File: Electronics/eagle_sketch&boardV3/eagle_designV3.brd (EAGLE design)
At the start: 134.6 x 61.9 mm, 16 parts, among them IC1 7805L

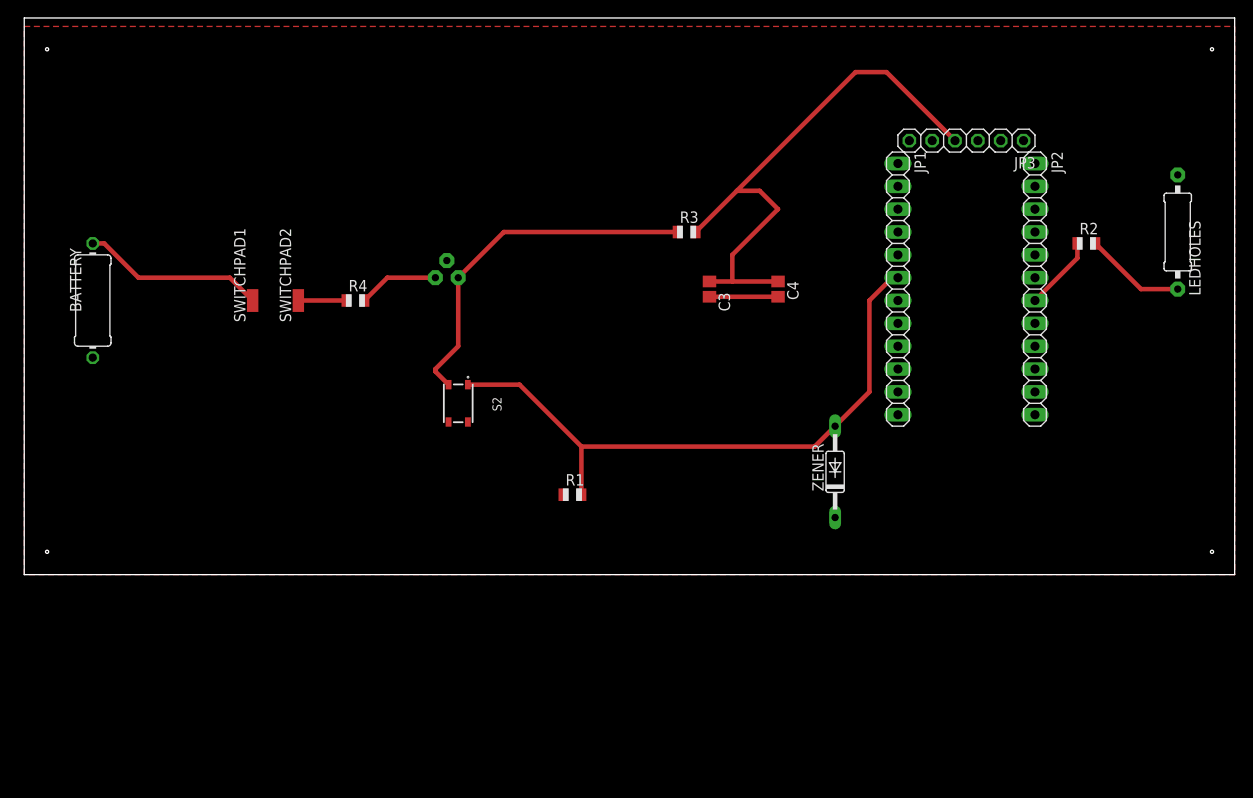
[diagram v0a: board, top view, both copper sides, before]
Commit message: updated board and schematic with post review suggestions from Issue 30
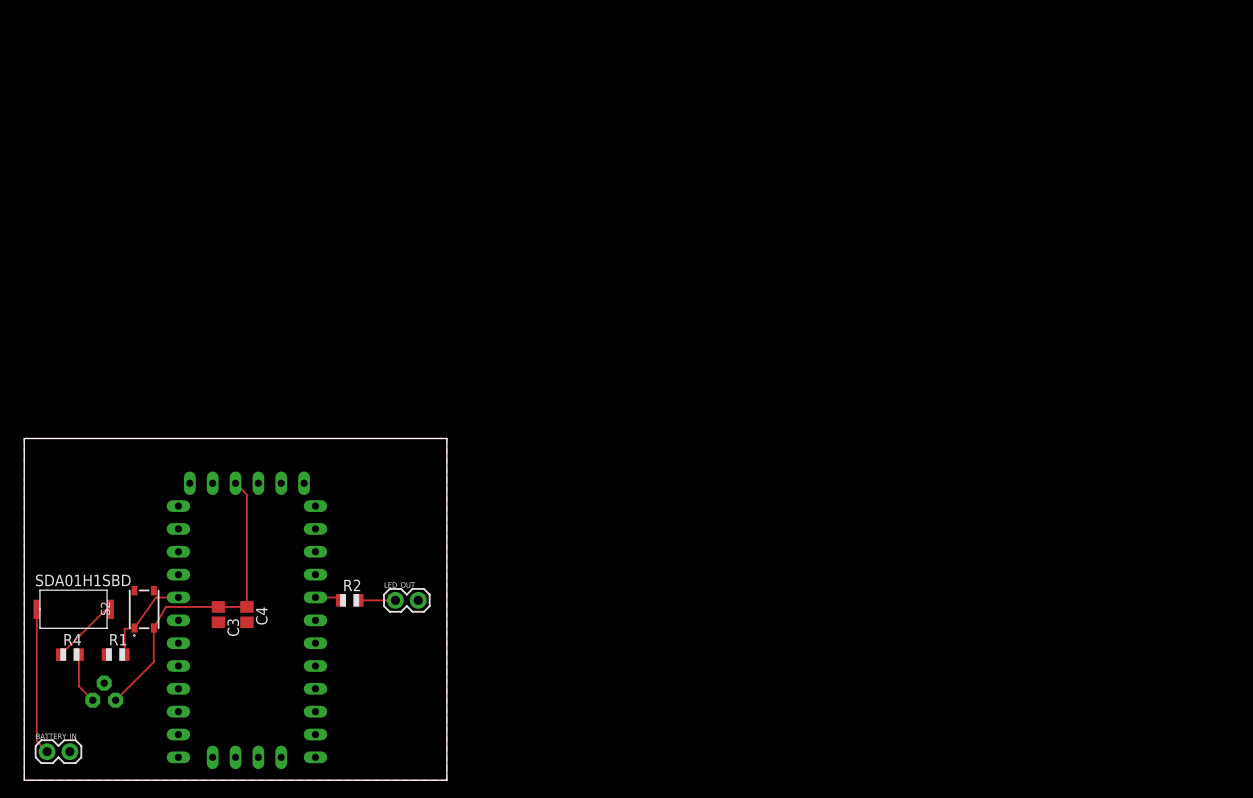
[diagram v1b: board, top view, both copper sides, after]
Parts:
- removed BATTERY: (no value), adafruit:0411/12
- removed JP1, JP2: (no value), adafruit:1X12
- removed JP3: (no value), adafruit:1X06
- removed LEDHOLES: (no value), adafruit:0309/12
- removed R3: 20k, adafruit:R0805
- removed SWITCHPAD1, SWITCHPAD2: (no value), wirepad:SMD1,27-2,54
- removed ZENER: 1N4446, diode:DO35-10
- added BATTERY_IN, LED_OUT: (no value), SparkFun-Connectors:1X02
- added U$1: PRO-MINI, Arduino-clone:PRO-MINI
- added U$2: SDA01H1SBD_DEVICE, DIPswitchLib:SDA01H1SBD_PART
- moved R2 91.0 mm to (36.2, 20.0)
- moved C4 69.3 mm to (24.8, 18.4)
- moved C3 65.5 mm to (21.6, 18.4)
- moved IC1 60.5 mm to (8.89, 8.89)
- moved R1 53.8 mm to (10.2, 14.0)
- moved R4 50.6 mm to (5.08, 14.0)
- moved S2 41.8 mm to (13.3, 19.0), turned to 90 degrees
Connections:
- removed net N$6: C3.1, C4.1, JP3.4, R3.2
- removed net N$9: LEDHOLES.2, R2.2
- new net N$7: LED_OUT.1, R2.2
- new net RAW: U$1.RAW
- net GND: now also BATTERY_IN.2, LED_OUT.2, U$1.GND; no longer BATTERY.1, JP2.2, LEDHOLES.1, ZENER.C
- net N$1: now also BATTERY_IN.1, U$2.OFF; no longer BATTERY.2, SWITCHPAD1.1
- net N$2: now also U$2.ON; no longer SWITCHPAD2.1
- net N$4: now also C3.1, C4.1, U$1.VCC1; no longer R3.1
- net N$5: now also U$1.D2; no longer JP1.6, ZENER.A
- net N$8: now also U$1.A3; no longer JP2.7
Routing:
- net N$6: track 62.6 -> 0.00 mm
- net N$5: track 69.8 -> 10.6 mm
- net N$9: track 11.3 -> 0.00 mm
- net GND: track 7.62 -> 0.00 mm
- net N$8: track 8.30 -> 2.94 mm
- net N$4: track 40.1 -> 35.8 mm
- net N$1: track 20.4 -> 16.3 mm
- net N$7: track 0.00 -> 4.08 mm
- net N$3: track 8.94 -> 5.72 mm
- net N$2: track 5.35 -> 8.32 mm
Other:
- board size 134.6 x 61.9 mm -> 47 x 38 mm

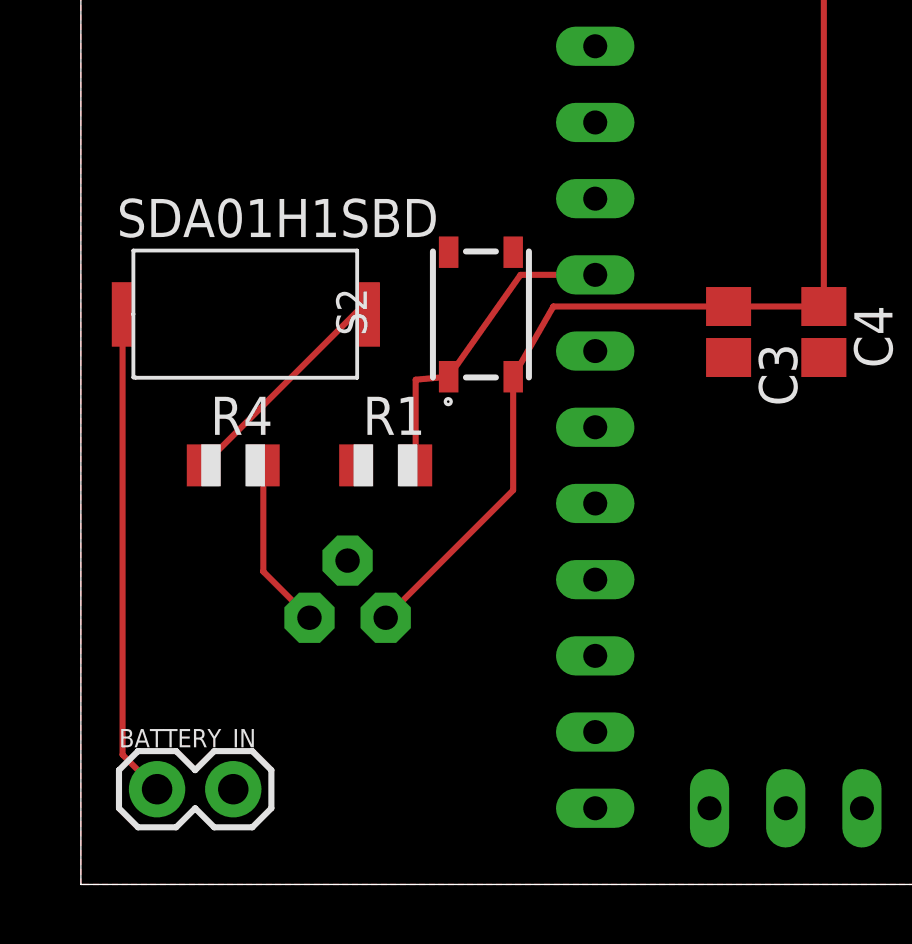
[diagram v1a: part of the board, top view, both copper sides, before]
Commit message: updated board to reflect toggle switch change
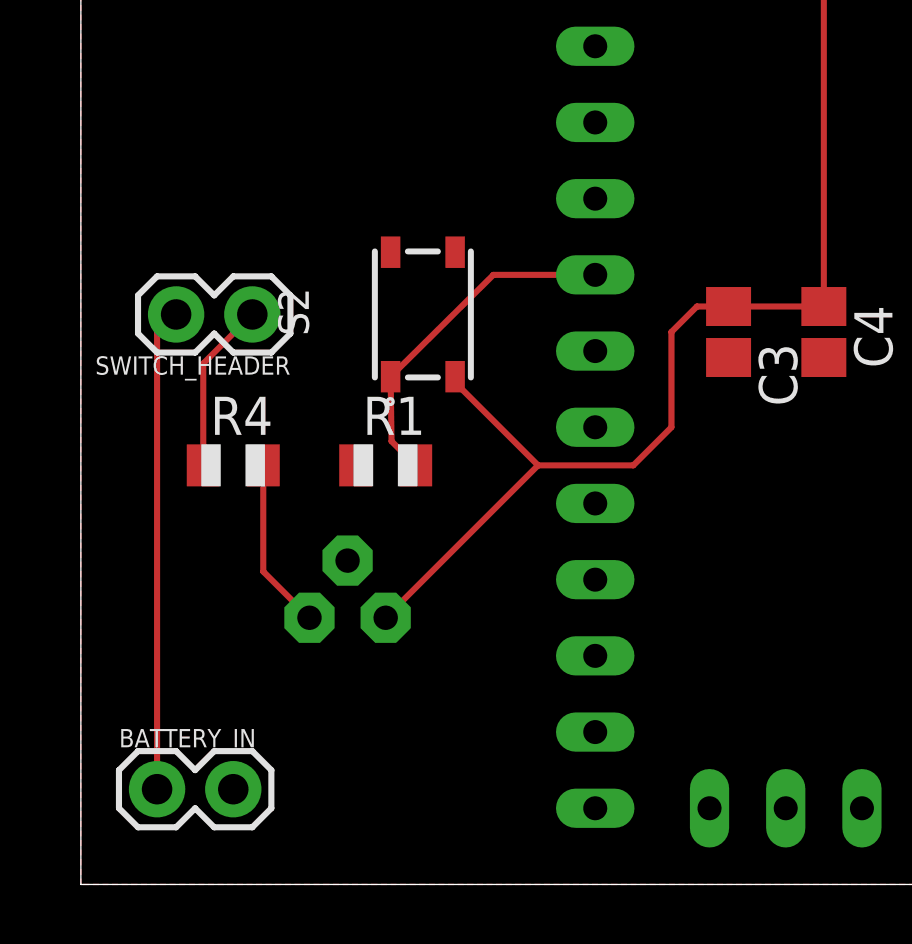
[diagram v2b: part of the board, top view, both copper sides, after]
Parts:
- removed U$2: SDA01H1SBD_DEVICE, DIPswitchLib:SDA01H1SBD_PART
- added SWITCH_HEADER: (no value), SparkFun-Connectors:1X02
- moved S2 1.94 mm to (11.4, 19.0)
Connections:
- net N$1: now also SWITCH_HEADER.2; no longer U$2.OFF
- net N$2: now also SWITCH_HEADER.1; no longer U$2.ON
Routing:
- net N$4: track 35.8 -> 39.1 mm
- net N$2: track 8.32 -> 5.71 mm
- net N$5: track 10.6 -> 11.5 mm
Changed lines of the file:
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@@
 <attribute name="VALUE" x="4.318" y="11.684" size="1.27" layer="27"/>
 </element>
-<element name="S2" library="SKRPABE010" package="SMT(4.2X3.2)" value="SKRPABE010" x="13.335" y="19" smashed="yes" rot="R90">
-<attribute name="DESCRIPTION" value="Switch Tactile 4.2 x 3.2mm SMT 1.57N Black Button Tactile Switch, SPST-NO 0.05 A 0.7mm" x="19.685" y="45.67" size="1.778" layer="27" rot="R90" display="off"/>
-<attribute name="HEIGHT" value="mm" x="13.335" y="19" size="1.778" layer="27" rot="R90" display="off"/>
-<attribute name="MANUFACTURER_NAME" value="ALPS" x="13.335" y="19" size="1.778" layer="27" rot="R90" display="off"/>
-<attribute name="MANUFACTURER_PART_NUMBER" value="SKRPABE010" x="13.335" y="19" size="1.778" layer="27" rot="R90" display="off"/>
-<attribute name="MOUSER_PART_NUMBER" value="688-SKRPAB" x="13.335" y="19" size="1.778" layer="27" rot="R90" display="off"/>
-<attribute name="NAME" x="9.53378125" y="18.290684375" size="1.017590625" layer="25" rot="R90"/>
-<attribute name="VALUE" x="18.31168125" y="18.163703125" size="1.01628125" layer="27" rot="R90"/>
+<element name="S2" library="SKRPABE010" package="SMT(4.2X3.2)" value="SKRPABE010" x="11.4" y="19" smashed="yes" rot="R90">
+<attribute name="DESCRIPTION" value="Switch Tactile 4.2 x 3.2mm SMT 1.57N Black Button Tactile Switch, SPST-NO 0.05 A 0.7mm" x="17.75" y="45.67" size="1.778" layer="27" rot="R90" display="off"/>
+<attribute name="HEIGHT" value="mm" x="11.4" y="19" size="1.778" layer="27" rot="R90" display="off"/>
+<attribute name="MANUFACTURER_NAME" value="ALPS" x="11.4" y="19" size="1.778" layer="27" rot="R90" display="off"/>
+<attribute name="MANUFACTURER_PART_NUMBER" value="SKRPABE010" x="11.4" y="19" size="1.778" layer="27" rot="R90" display="off"/>
+<attribute name="MOUSER_PART_NUMBER" value="688-SKRPAB" x="11.4" y="19" size="1.778" layer="27" rot="R90" display="off"/>
+<attribute name="NAME" x="7.59878125" y="18.290684375" size="1.017590625" layer="25" rot="R90"/>
+<attribute name="VALUE" x="16.37668125" y="18.163703125" size="1.01628125" layer="27" rot="R90"/>
 </element>
 <element name="U$1" library="Arduino-clone" package="PRO-MINI" value="PRO-MINI" x="23.495" y="3.81" smashed="yes"/>
-<element name="U$2" library="DIPswitchLib" package="SDA01H1SBD_PART" value="SDA01H1SBD_DEVICE" x="5.5" y="19" smashed="yes"/>
 <element name="BATTERY_IN" library="SparkFun-Connectors" library_urn="urn:adsk.eagle:library:513" package="1X02" package3d_urn="urn:adsk.eagle:package:38039/1" value="" x="2.54" y="3.175" smashed="yes">
 <attribute name="NAME" x="1.27" y="4.572" size="0.6096" layer="25" font="vector" ratio="20"/>
@@
 <attribute name="VALUE" x="40.005" y="17.968" size="0.6096" layer="27" font="vector" ratio="20"/>
 </element>
+<element name="SWITCH_HEADER" library="SparkFun-Connectors" library_urn="urn:adsk.eagle:library:513" package="1X02" package3d_urn="urn:adsk.eagle:package:38039/1" value="" x="5.715" y="19" smashed="yes" rot="R180">
+<attribute name="NAME" x="6.985" y="17.603" size="0.6096" layer="25" font="vector" ratio="20" rot="R180"/>
+<attribute name="VALUE" x="6.985" y="21.032" size="0.6096" layer="27" font="vector" ratio="20" rot="R180"/>
+</element>
 </elements>
 <signals>
 <signal name="N$2">
 <contactref element="R4" pad="1"/>
-<contactref element="U$2" pad="ON"/>
-<wire x1="4.08" y1="13.97" x2="9.61" y2="19.5" width="0.2032" layer="1"/>
-<wire x1="9.61" y1="19.5" x2="9.61" y2="19" width="0.2032" layer="1"/>
+<contactref element="SWITCH_HEADER" pad="1"/>
+<wire x1="5.715" y1="19" x2="4.08" y2="17.365" width="0.2032" layer="1"/>
+<wire x1="4.08" y1="17.365" x2="4.08" y2="13.97" width="0.2032" layer="1"/>
 </signal>
 <signal name="N$3">
@@
 <contactref element="C4" pad="1"/>
 <contactref element="U$1" pad="VCC1"/>
-<wire x1="10.16" y1="8.89" x2="14.41" y2="13.14" width="0.2032" layer="1"/>
-<wire x1="14.41" y1="13.14" x2="14.41" y2="16.925" width="0.2032" layer="1"/>
 <wire x1="21.59" y1="19.265" x2="24.765" y2="19.265" width="0.2032" layer="1"/>
-<wire x1="14.41" y1="16.925" x2="15.75" y2="19.265" width="0.2032" layer="1"/>
-<wire x1="15.75" y1="19.265" x2="21.59" y2="19.265" width="0.2032" layer="1"/>
 <wire x1="24.765" y1="19.265" x2="24.765" y2="31.75" width="0.2032" layer="1"/>
 <wire x1="24.765" y1="31.75" x2="23.495" y2="33.02" width="0.2032" layer="1"/>
+<wire x1="10.16" y1="8.89" x2="15.24" y2="13.97" width="0.2032" layer="1"/>
+<wire x1="15.24" y1="13.97" x2="18.415" y2="13.97" width="0.2032" layer="1"/>
+<wire x1="18.415" y1="13.97" x2="19.685" y2="15.24" width="0.2032" layer="1"/>
+<wire x1="19.685" y1="15.24" x2="19.685" y2="18.415" width="0.2032" layer="1"/>
+<wire x1="19.685" y1="18.415" x2="20.535" y2="19.265" width="0.2032" layer="1"/>
+<wire x1="20.535" y1="19.265" x2="21.59" y2="19.265" width="0.2032" layer="1"/>
+<wire x1="15.24" y1="13.97" x2="12.505" y2="16.705" width="0.2032" layer="1"/>
+<wire x1="12.505" y1="16.705" x2="12.475" y2="16.925" width="0.2032" layer="1"/>
 </signal>
 <signal name="N$5">
@@
 <contactref element="R1" pad="2"/>
 <contactref element="U$1" pad="D2"/>
-<wire x1="12.26" y1="16.925" x2="11.16" y2="16.825" width="0.2032" layer="1"/>
-<wire x1="11.16" y1="16.825" x2="11.16" y2="13.97" width="0.2032" layer="1"/>
-<wire x1="12.26" y1="16.925" x2="14.655" y2="20.32" width="0.2032" layer="1"/>
-<wire x1="14.655" y1="20.32" x2="17.145" y2="20.32" width="0.2032" layer="1"/>
+<wire x1="11.16" y1="13.97" x2="10.355" y2="14.775" width="0.2032" layer="1"/>
+<wire x1="10.355" y1="14.775" x2="10.325" y2="16.925" width="0.2032" layer="1"/>
+<wire x1="10.325" y1="16.925" x2="13.75" y2="20.32" width="0.2032" layer="1"/>
+<wire x1="13.75" y1="20.32" x2="17.145" y2="20.32" width="0.2032" layer="1"/>
 </signal>
 <signal name="N$8">
@@
 <signal name="N$1">
 <contactref element="BATTERY_IN" pad="1"/>
-<contactref element="U$2" pad="OFF"/>
-<wire x1="2.54" y1="3.175" x2="1.39" y2="4.325" width="0.2032" layer="1"/>
-<wire x1="1.39" y1="4.325" x2="1.39" y2="19" width="0.2032" layer="1"/>
+<contactref element="SWITCH_HEADER" pad="2"/>
+<wire x1="2.54" y1="3.175" x2="2.54" y2="18.365" width="0.2032" layer="1"/>
+<wire x1="2.54" y1="18.365" x2="3.175" y2="19" width="0.2032" layer="1"/>
 </signal>
 <signal name="N$7">

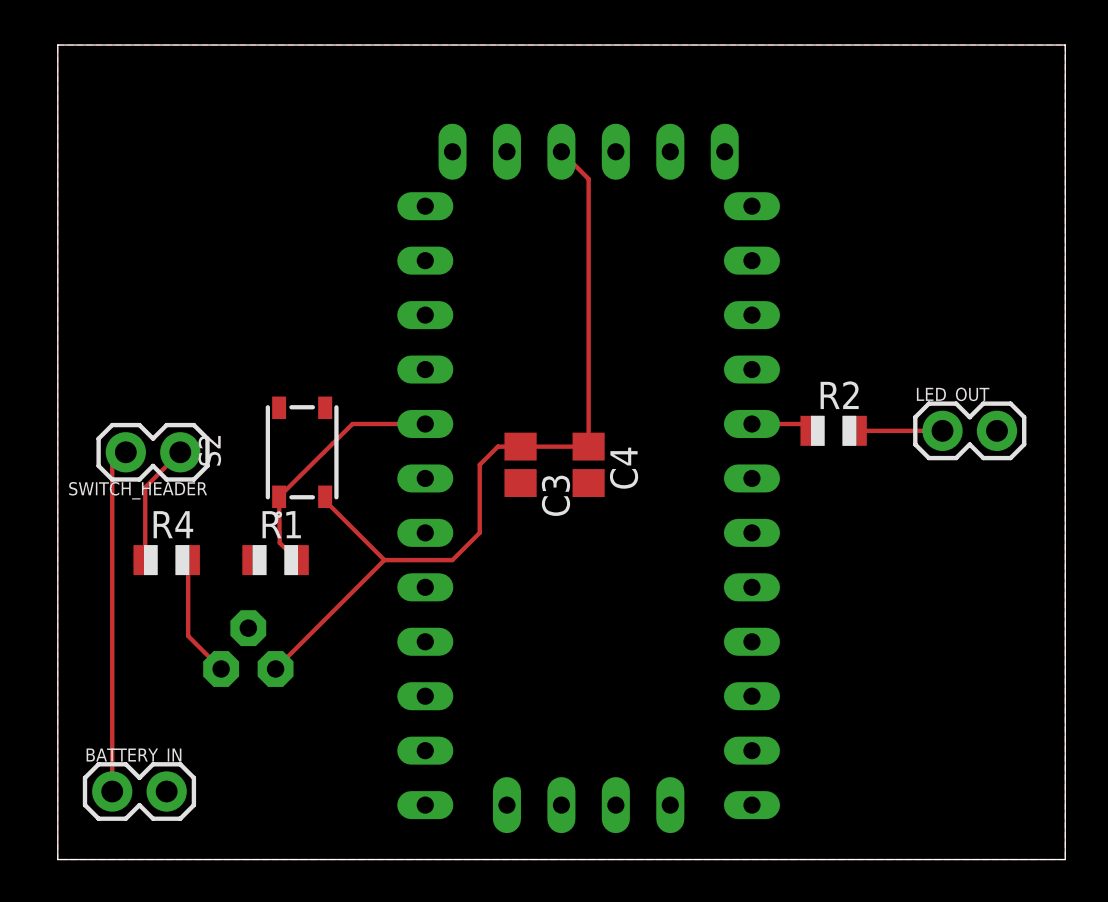
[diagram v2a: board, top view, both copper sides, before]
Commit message: updated board and schematic to reflect removal of resistor btwn battery and voltage reg
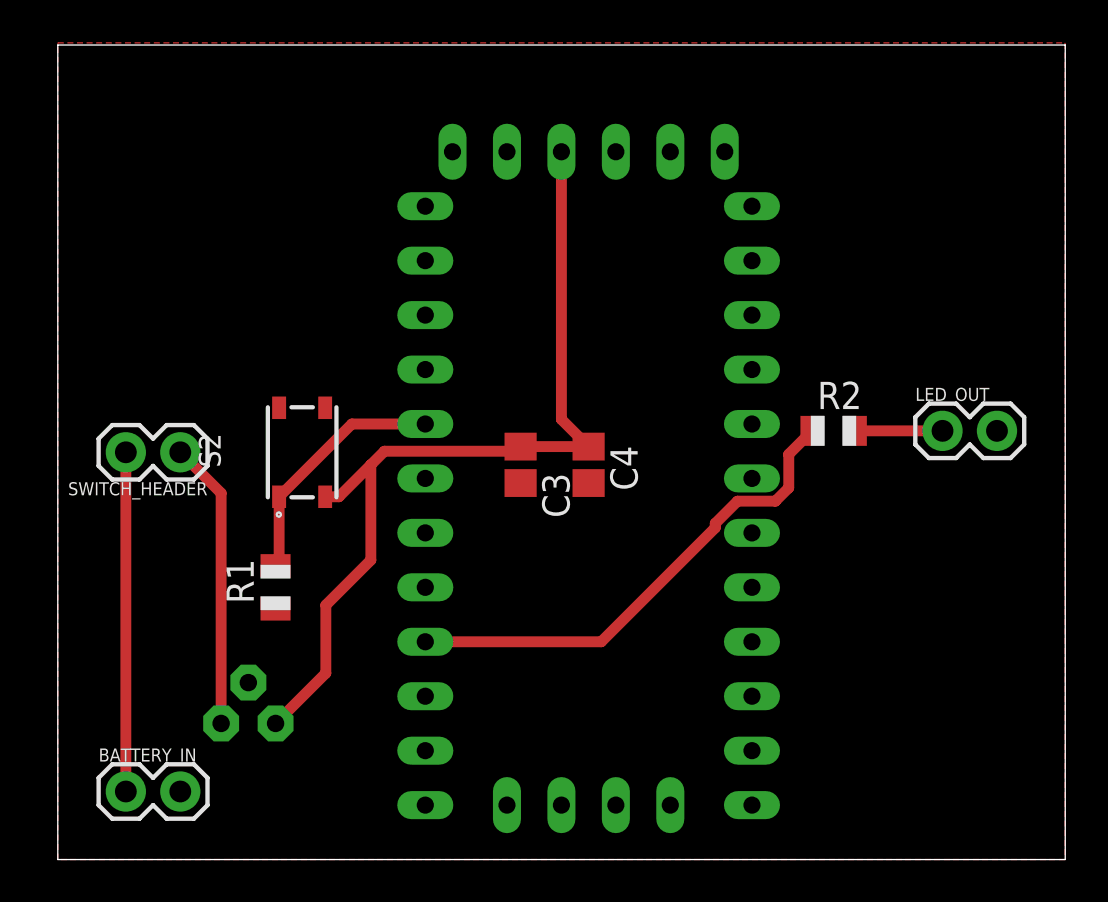
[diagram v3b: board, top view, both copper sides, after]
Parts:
- removed R4: 20k, adafruit:R0805
- R2: value 1.5k -> 330
- moved IC1 2.54 mm to (8.89, 6.35)
- moved R1 1.27 mm to (10.2, 12.7), turned to 90 degrees
- moved BATTERY_IN 0.63 mm to (3.17, 3.17)
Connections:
- removed net N$3: IC1.3, R4.2
- removed net N$8: R2.1, U$1.A3
- new net N$6: R2.1, U$1.D6
- net N$2: now also IC1.3; no longer R4.1
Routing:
- net N$6: track 0.00 -> 23.2 mm
- net N$2: track 5.71 -> 13.4 mm
- net N$3: track 5.72 -> 0.00 mm
- net N$8: track 2.94 -> 0.00 mm
- net N$4: track 39.1 -> 41.7 mm
